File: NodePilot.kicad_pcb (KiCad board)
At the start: 2 copper layers, 100 x 55 mm, 50 parts, among them K1 SRD-05VDC-SL-C, Q1 2N3904, Q2 2N2222, Q4 2N3904, T1 1:1 600R, T2 1:1 600R, U1 PC817, U2 PC817, U3 B0505S-1WR2

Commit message: release commit with text
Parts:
- moved ? 8.73 mm to (80.5, 40.0), turned to 0 degrees
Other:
- board text added: "NodePilot Advanced"
- board text added: "Rev 2.3"
- board text added: "S21TIP"
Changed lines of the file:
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@@
 	(footprint "logo:node_pilot_logo"
 		(layer "F.Cu")
-		(at 82.5 48.5 -90)
+		(at 80.5 40)
 		(property "Reference" ""
-			(at 0 0 90)
+			(at 0 0 0)
 			(layer "F.SilkS")
 			(effects
@@
 		)
 		(property "Value" "LOGO"
-			(at 0.75 0 90)
+			(at 0.75 0 0)
 			(layer "F.SilkS")
 			(hide yes)
@@
 		)
 		(property "Datasheet" ""
-			(at 0 0 90)
+			(at 0 0 0)
 			(layer "F.Fab")
 			(hide yes)
@@
 		)
 		(property "Description" ""
-			(at 0 0 90)
+			(at 0 0 0)
 			(layer "F.Fab")
 			(hide yes)
@@
 		(fp_poly
 			(pts
-				(xy 1.535445 1.22711) (xy 1.6194 1.287923) (xy 1.652195 1.369019) (xy 1.631375 1.424225) (xy 1.538238 1.481943)
-				(xy 1.483847 1.491288) (xy 1.395967 1.531296) (xy 1.346808 1.599526) (xy 1.321243 1.644384) (xy 1.31011 1.612372)
-				(xy 1.311132 1.494757) (xy 1.312279 1.467235) (xy 1.320439 1.371911) (xy 1.350859 1.371911) (xy 1.37904 1.411111)
-				(xy 1.456948 1.443417) (xy 1.542055 1.429338) (xy 1.587031 1.377974) (xy 1.587499 1.371023) (xy 1.545681 1.312987)
-				(xy 1.467234 1.298864) (xy 1.367962 1.31884) (xy 1.350859 1.371911) (xy 1.320439 1.371911) (xy 1.324823 1.320689)
-				(xy 1.353047 1.245048) (xy 1.408104 1.215108) (xy 1.425158 1.212118)
+				(xy -0.432955 -0.55322) (xy -0.432955 0.24053) (xy -0.619858 0.24053) (xy -0.806761 0.24053) (xy -1.136998 -0.348769)
+				(xy -1.467236 -0.938068) (xy -1.480743 -0.348769) (xy -1.49425 0.24053) (xy -1.637087 0.24053) (xy -1.779925 0.24053)
+				(xy -1.779925 -0.55322) (xy -1.779925 -1.34697) (xy -1.575474 -1.345941) (xy -1.371023 -1.344912)
+				(xy -1.058334 -0.769697) (xy -0.942572 -0.559734) (xy -0.842551 -0.383935) (xy -0.767308 -0.257765)
+				(xy -0.725878 -0.196691) (xy -0.721592 -0.193362) (xy -0.713468 -0.237892) (xy -0.709002 -0.36005)
+				(xy -0.708491 -0.541311) (xy -0.712229 -0.763148) (xy -0.712394 -0.769606) (xy -0.727249 -1.34697)
+				(xy -0.580102 -1.34697) (xy -0.432955 -1.34697)
 			)
 			(stroke
@@
 		(fp_poly
 			(pts
-				(xy -0.432955 -0.55322) (xy -0.432955 0.24053) (xy -0.619858 0.24053) (xy -0.806761 0.24053) (xy -1.136998 -0.348769)
-				(xy -1.467236 -0.938068) (xy -1.480743 -0.348769) (xy -1.49425 0.24053) (xy -1.637087 0.24053) (xy -1.779925 0.24053)
-				(xy -1.779925 -0.55322) (xy -1.779925 -1.34697) (xy -1.575474 -1.345941) (xy -1.371023 -1.344912)
-				(xy -1.058334 -0.769697) (xy -0.942572 -0.559734) (xy -0.842551 -0.383935) (xy -0.767308 -0.257765)
-				(xy -0.725878 -0.196691) (xy -0.721592 -0.193362) (xy -0.713468 -0.237892) (xy -0.709002 -0.36005)
-				(xy -0.708491 -0.541311) (xy -0.712229 -0.763148) (xy -0.712394 -0.769606) (xy -0.727249 -1.34697)
-				(xy -0.580102 -1.34697) (xy -0.432955 -1.34697)
+				(xy 1.535445 1.22711) (xy 1.6194 1.287923) (xy 1.652195 1.369019) (xy 1.631375 1.424225) (xy 1.538238 1.481943)
+				(xy 1.483847 1.491288) (xy 1.395967 1.531296) (xy 1.346808 1.599526) (xy 1.321243 1.644384) (xy 1.31011 1.612372)
+				(xy 1.311132 1.494757) (xy 1.312279 1.467235) (xy 1.320439 1.371911) (xy 1.350859 1.371911) (xy 1.37904 1.411111)
+				(xy 1.456948 1.443417) (xy 1.542055 1.429338) (xy 1.587031 1.377974) (xy 1.587499 1.371023) (xy 1.545681 1.312987)
+				(xy 1.467234 1.298864) (xy 1.367962 1.31884) (xy 1.350859 1.371911) (xy 1.320439 1.371911) (xy 1.324823 1.320689)
+				(xy 1.353047 1.245048) (xy 1.408104 1.215108) (xy 1.425158 1.212118)
 			)
 			(stroke
@@
 		(layer "Edge.Cuts")
 	)
+	(gr_text "Rev 2.3"
+		(at 64.5 85 90)
+		(layer "F.SilkS")
+		(effects
+			(font
+				(size 1 1)
+				(thickness 0.2)
+			)
+			(justify left bottom)
+		)
+	)
+	(gr_text "S21TIP"
+		(at 62.5 85 90)
+		(layer "F.SilkS")
+		(effects
+			(font
+				(size 1.2 1.2)
+				(thickness 0.3)
+				(bold yes)
+			)
+			(justify left bottom)
+		)
+	)
+	(gr_text "NodePilot Advanced"
+		(at 60 85 90)
+		(layer "F.SilkS")
+		(effects
+			(font
+				(size 1.5 1.5)
+				(thickness 0.3)
+				(bold yes)
+			)
+			(justify left bottom)
+		)
+	)
 	(segment
 		(start 86.5 57.96)
@@
 		(net "Net-(T1-SA)")
 	)
+	(group ""
+		(members "2bf5c958-4f0a-44af-bf77-4a6c3f6de93e" "eaee5705-09c5-41a4-bdfe-460ac92ee4a0"
+			"f17a26bf-60f9-4797-9a8b-59644c61c88d"
+		)
+	)
 	(embedded_fonts no)

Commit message: cosmetics
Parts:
- added REF**: OSHW-Logo2_7.3x6mm_SilkScreen, Symbol:OSHW-Logo2_7.3x6mm_SilkScreen, F.Cu at (75.5, 39.0)
- moved ? 7.28 mm to (82.5, 47.0), turned to -90 degrees
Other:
- board text added: "Rev 5.3"
- board text removed: "Rev 2.3"

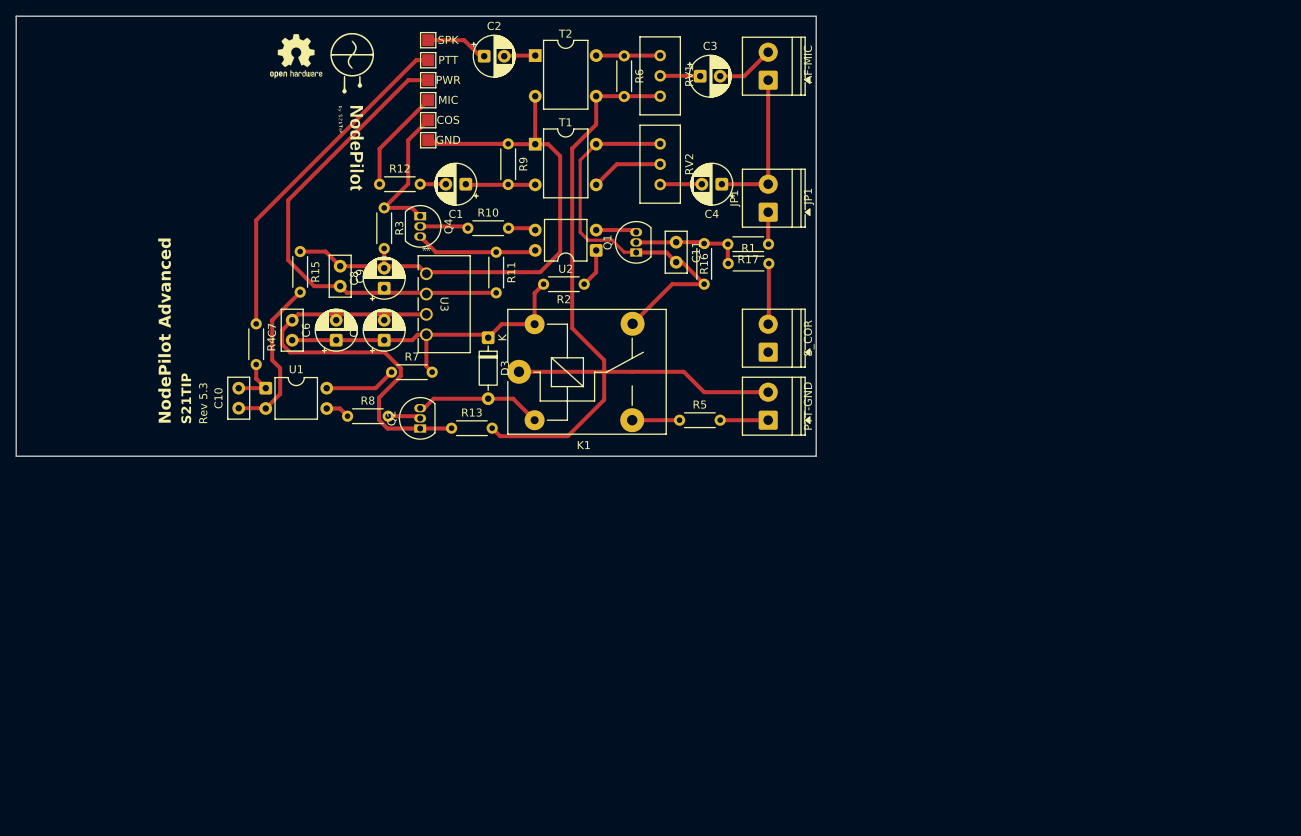
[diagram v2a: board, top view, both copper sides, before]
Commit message: fixing the transformer footprint
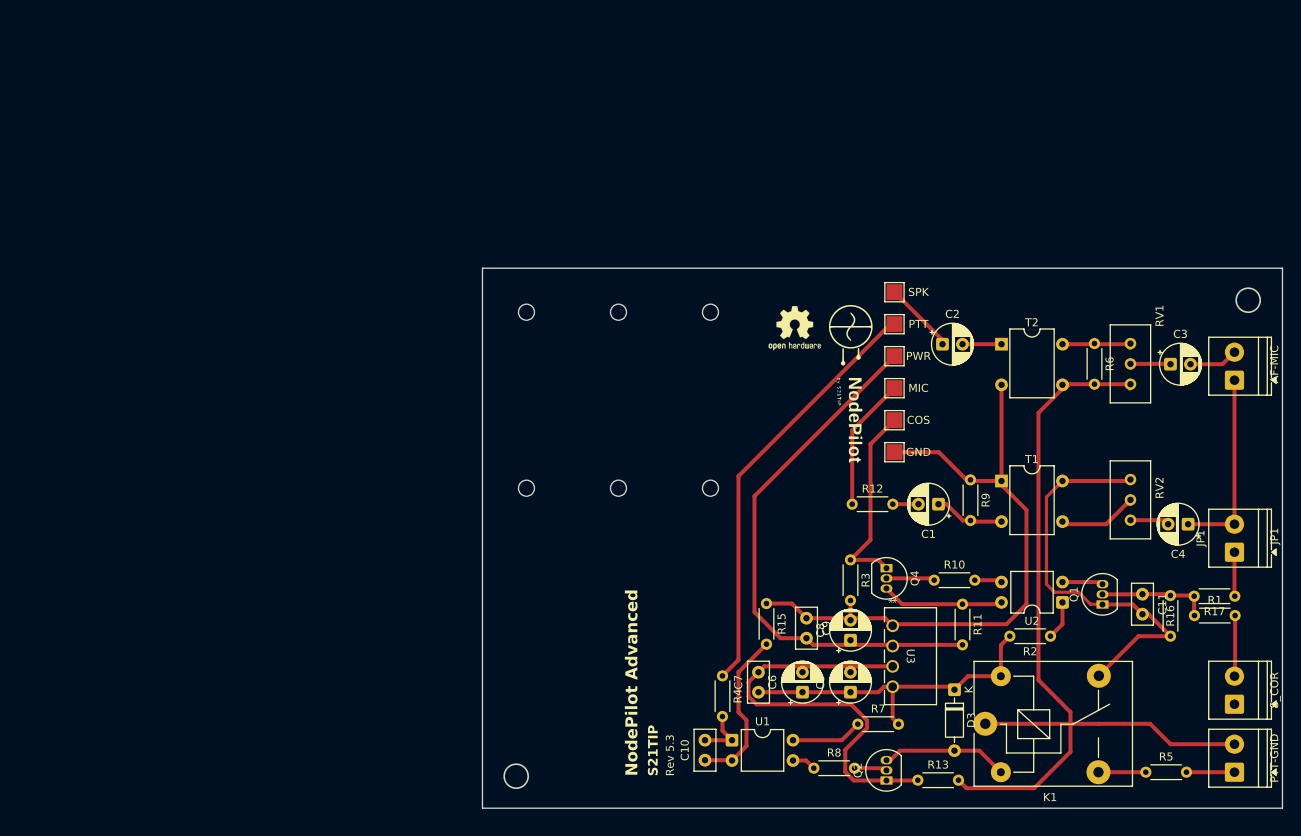
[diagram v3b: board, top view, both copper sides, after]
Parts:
- removed the ? at (92.0, 47.0)
- removed the ? at (92.0, 49.5)
- removed the ? at (92.0, 39.5)
- removed the ? at (92.0, 44.5)
- removed the ? at (134.5, 76.0)
- removed the ? at (92.0, 37.0)
- removed the ? at (134.5, 42.0)
- removed the ? at (134.5, 84.5)
- removed the ? at (92.0, 42.0)
- added ?: PWR, TestPoint:TestPoint_Pad_2.0x2.0mm, F.Cu at (150.3, 76.5)
- added ?: SPK, TestPoint:TestPoint_Pad_2.0x2.0mm, F.Cu at (150.3, 68.5)
- added ?: MIC, TestPoint:TestPoint_Pad_2.0x2.0mm, F.Cu at (150.3, 80.5)
- added ?: COS, TestPoint:TestPoint_Pad_2.0x2.0mm, F.Cu at (150.3, 84.5)
- added ?: S_COR, TerminalBlock_Phoenix:TerminalBlock_Phoenix_PT-1,5-2-3.5-H_1x02_P3.50mm_Horizontal, F.Cu at (192.8, 120.0)
- added ?: PTT, TestPoint:TestPoint_Pad_2.0x2.0mm, F.Cu at (150.3, 72.5)
- added ?: GND, TestPoint:TestPoint_Pad_2.0x2.0mm, F.Cu at (150.3, 88.5)
- added ?: PTT-GND, TerminalBlock_Phoenix:TerminalBlock_Phoenix_PT-1,5-2-3.5-H_1x02_P3.50mm_Horizontal, F.Cu at (192.8, 128.5)
- added ?: AF-MIC, TerminalBlock_Phoenix:TerminalBlock_Phoenix_PT-1,5-2-3.5-H_1x02_P3.50mm_Horizontal, F.Cu at (192.8, 79.5)
- moved C10 73.0 mm to (126.6, 127.0)
- moved C11 73.0 mm to (181.3, 106.2)
- moved C5 73.0 mm to (144.8, 118.5)
- moved C6 73.0 mm to (138.8, 118.5)
- moved C7 73.0 mm to (133.3, 118.5)
- moved C8 73.0 mm to (144.8, 112.0)
- moved C9 73.0 mm to (139.3, 109.2)
- moved D3 73.0 mm to (157.8, 118.2)
- moved K1 73.0 mm to (161.6, 122.5)
- moved Q1 73.0 mm to (176.3, 107.5)
- moved Q4 73.0 mm to (149.3, 103.0)
- moved R1 73.0 mm to (187.8, 108.9)
- moved R10 73.0 mm to (155.2, 104.5)
- moved R11 73.0 mm to (158.8, 107.5)
- moved R13 73.0 mm to (153.2, 129.5)
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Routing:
- net GPIO3: track 42.7 -> 53.2 mm
- net RIGGND: track 97.4 -> 105.5 mm
- net USBPWR: track 58.9 -> 66.9 mm
- net GROUND: track 73.6 -> 80.5 mm
- net VOLDN: track 18.2 -> 24.7 mm
- net RIGAF: track 18.8 -> 23.8 mm
- net MICIN: track 13.0 -> 16.7 mm
- net Net-(Q1-E): track 49.0 -> 52.3 mm
- net LOL: track 7.83 -> 9.49 mm
- net Net-(JP1-A): track 4.02 -> 5.52 mm
- net Net-(C3-Pad1): track 5.02 -> 6.22 mm
- net Net-(T2-AA): track 3.91 -> 5.09 mm
- net Net-(T2-SB): track 8.00 -> 8.64 mm
- net RIGMICIN: track 7.24 -> 6.62 mm
- net Net-(T1-SA): track 9.07 -> 9.61 mm
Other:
- board size 100 x 55 mm -> 100 x 67.5 mm

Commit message: board size fix
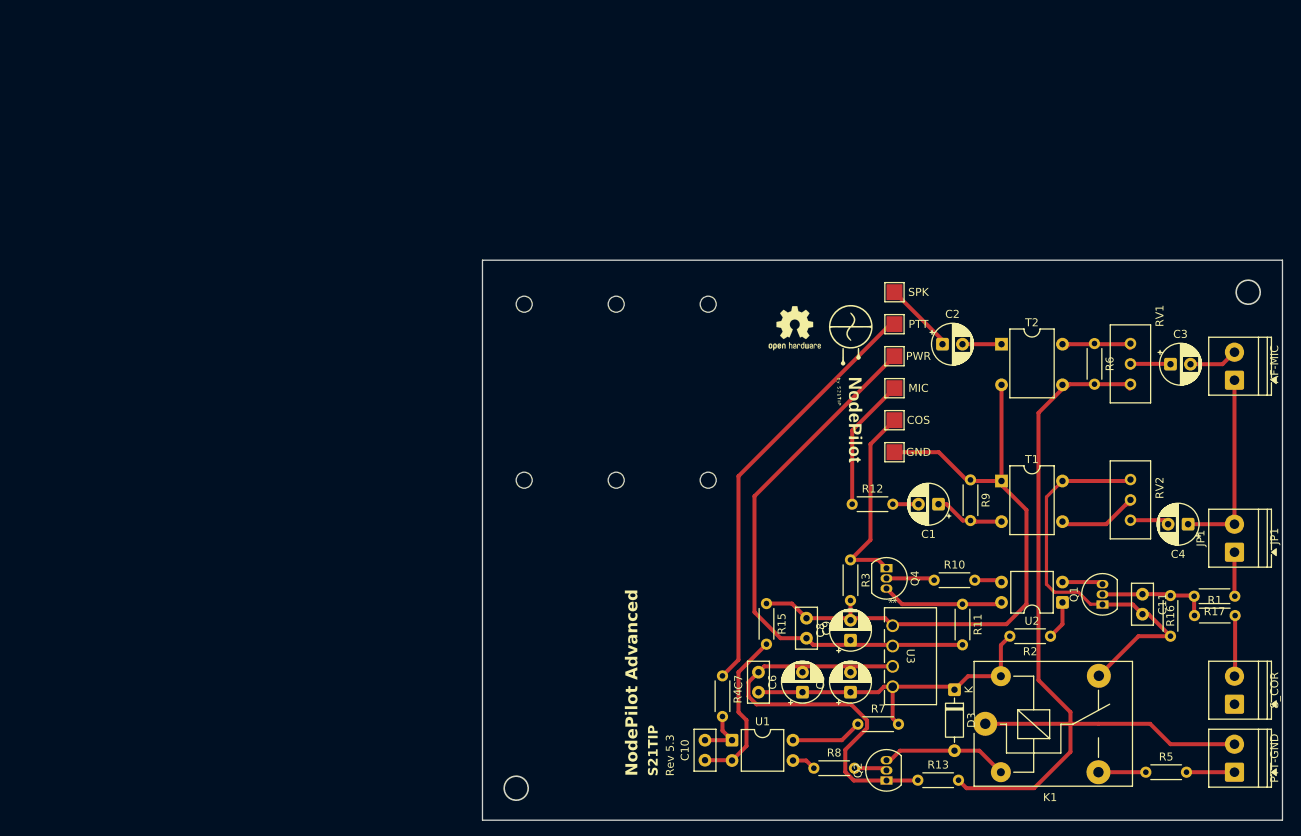
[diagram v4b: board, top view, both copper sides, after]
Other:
- board size 100 x 67.5 mm -> 100 x 70 mm
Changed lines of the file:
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@@
 	)
 	(gr_rect
-		(start 98.785113 65.5)
-		(end 198.785113 133)
+		(start 98.785113 64.5)
+		(end 198.785113 134.5)
 		(radius 1)
 		(stroke
@@
 	)
 	(gr_circle
-		(center 103 129)
-		(end 104.5 129)
+		(center 103 130.5)
+		(end 104.5 130.5)
 		(stroke
 			(width 0.2)
@@
 	)
 	(gr_circle
-		(center 104.285113 71)
-		(end 105.285113 71)
+		(center 104 70)
+		(end 105 70)
 		(stroke
 			(width 0.05)
@@
 	)
 	(gr_circle
-		(center 104.285113 93)
-		(end 105.285113 93)
+		(center 104 92)
+		(end 105 92)
 		(stroke
 			(width 0.05)
@@
 	)
 	(gr_circle
-		(center 115.785113 71)
-		(end 116.785113 71)
+		(center 115.5 70)
+		(end 116.5 70)
 		(stroke
 			(width 0.05)
@@
 	)
 	(gr_circle
-		(center 115.785113 93)
-		(end 116.785113 93)
+		(center 115.5 92)
+		(end 116.5 92)
 		(stroke
 			(width 0.05)
@@
 	)
 	(gr_circle
-		(center 127.285113 71)
-		(end 128.285113 71)
+		(center 127 70)
+		(end 128 70)
 		(stroke
 			(width 0.05)
@@
 	)
 	(gr_circle
-		(center 127.285113 93)
-		(end 128.285113 93)
+		(center 127 92)
+		(end 128 92)
 		(stroke
 			(width 0.05)
@@
 	)
 	(gr_circle
-		(center 194.5 69.5)
-		(end 196 69.5)
+		(center 194.5 68.5)
+		(end 196 68.5)
 		(stroke
 			(width 0.2)

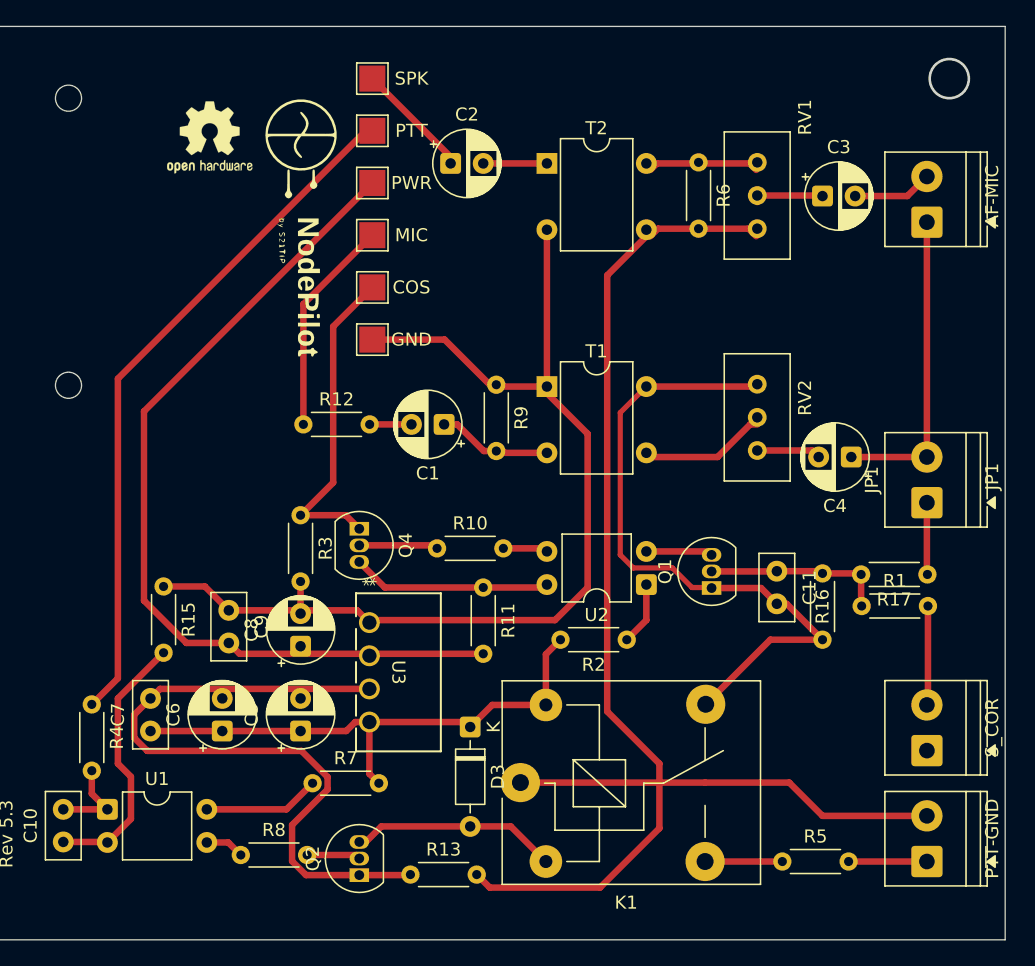
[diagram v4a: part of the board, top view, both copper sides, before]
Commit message: footprint fix
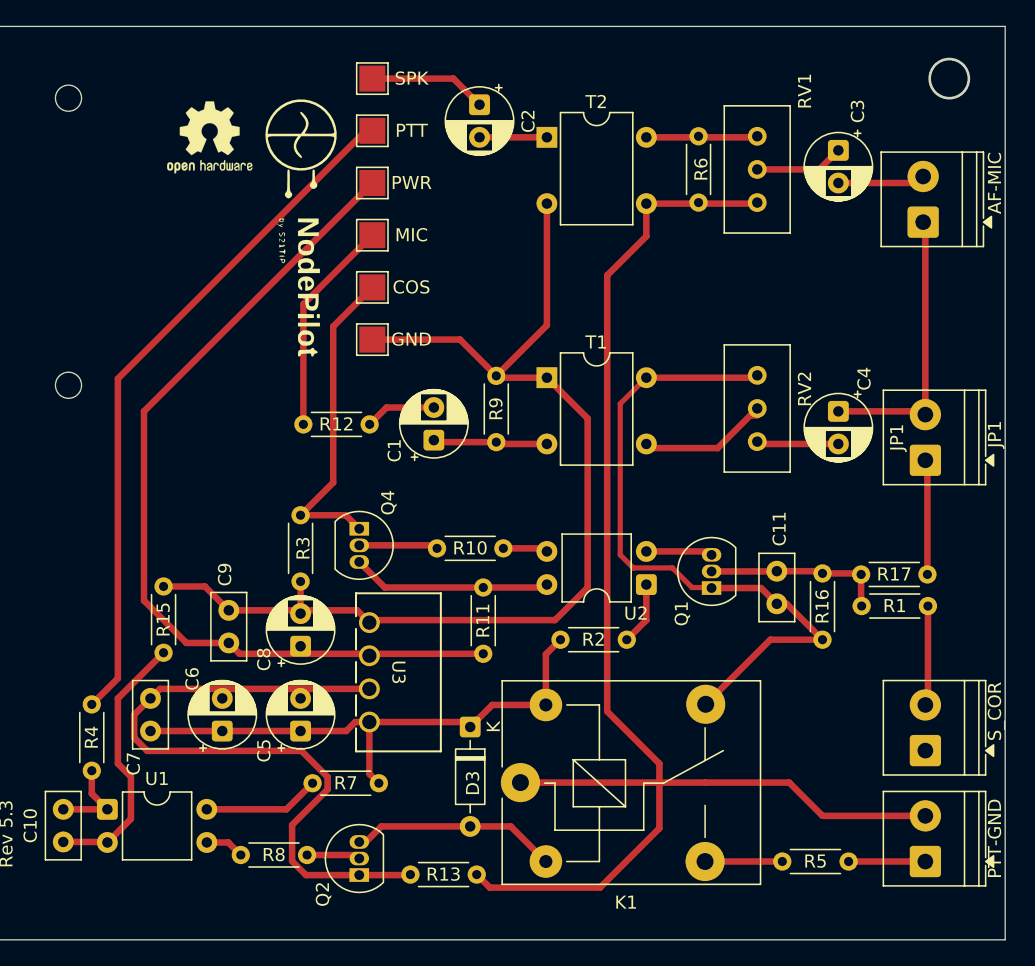
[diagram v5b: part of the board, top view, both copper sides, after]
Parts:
- moved C2 5.02 mm to (158.5, 70.5), turned to -90 degrees
- moved C3 3.70 mm to (186.0, 74.0), turned to -90 degrees
- moved C4 3.64 mm to (186.0, 94.0), turned to -90 degrees
- moved JP1 3.25 mm to (192.7, 97.8)
- moved R6 2.00 mm to (175.3, 72.9)
- moved RV1 2.00 mm to (179.8, 78.0)
- moved T2 2.00 mm to (163.7, 73.0)
- moved C1 1.44 mm to (155.0, 96.2), turned to 90 degrees
- moved RV2 0.68 mm to (179.8, 96.3)
- moved R9 0.68 mm to (159.8, 91.3)
- moved T1 0.68 mm to (163.7, 91.4)
- moved ? 0.29 mm to (192.5, 79.5)
- moved ? 0.12 mm to (192.7, 120.0)
- moved ? 0.12 mm to (192.7, 128.5)
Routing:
- net GROUND: track 80.5 -> 84.5 mm
- net Net-(JP1-A): track 5.52 -> 8.87 mm
- net RIGGND: track 105.5 -> 107.8 mm
- net Net-(C1-Pad2): track 3.21 -> 5.46 mm
- net RIGAF: track 23.8 -> 21.6 mm
- net Net-(C4-Pad2): track 4.91 -> 6.29 mm
- net RIGMICIN: track 6.62 -> 7.49 mm
- net Net-(C3-Pad1): track 6.22 -> 6.93 mm
- net Net-(Q1-E): track 52.3 -> 53.0 mm

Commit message: GP introduced
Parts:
- renumbered REF** to ?
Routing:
- added copper zone on B.Cu, net GROUND
- added copper zone on F.Cu, net GROUND
- added copper zone on B.Cu, net RIGGND
- added copper zone on F.Cu, net RIGGND
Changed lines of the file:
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@@
 		(capping no)
 		(filling no)
+		(zone_defaults)
 		(pcbplotparams
 			(layerselection 0x00000000_00000000_55555555_5755f5ff)
@@
 		(descr "Open Source Hardware Symbol")
 		(tags "Logo Symbol OSHW")
-		(property "Reference" "REF**"
+		(property "Reference" ""
 			(at 0 0 0)
 			(layer "F.SilkS")
@@
 		(net "Net-(K1-Pad3)")
 	)
+	(zone
+		(net "RIGGND")
+		(layers "F.Cu" "B.Cu")
+		(hatch edge 0.5)
+		(connect_pads
+			(clearance 0.5)
+		)
+		(min_thickness 0.25)
+		(fill yes
+			(thermal_gap 0.5)
+			(thermal_bridge_width 0.5)
+			(island_removal_mode 0)
+		)
+		(polygon
+			(pts
+				(xy 168 114) (xy 168 65.5) (xy 198 65.5) (xy 198 133.5) (xy 160 133.5) (xy 160 114)
+			)
+		)
+	)
+	(zone
+		(net "GROUND")
+		(layers "F.Cu" "B.Cu")
+		(hatch edge 0.5)
+		(priority 1)
+		(connect_pads
+			(clearance 0.5)
+		)
+		(min_thickness 0.25)
+		(fill yes
+			(thermal_gap 0.5)
+			(thermal_bridge_width 0.5)
+			(island_removal_mode 0)
+		)
+		(polygon
+			(pts
+				(xy 167 113) (xy 167 65.5) (xy 145 65.5) (xy 120 90) (xy 120 133.5) (xy 159 133.5) (xy 159 113)
+			)
+		)
+	)
 	(group ""
